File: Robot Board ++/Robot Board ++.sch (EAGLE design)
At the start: 39 parts

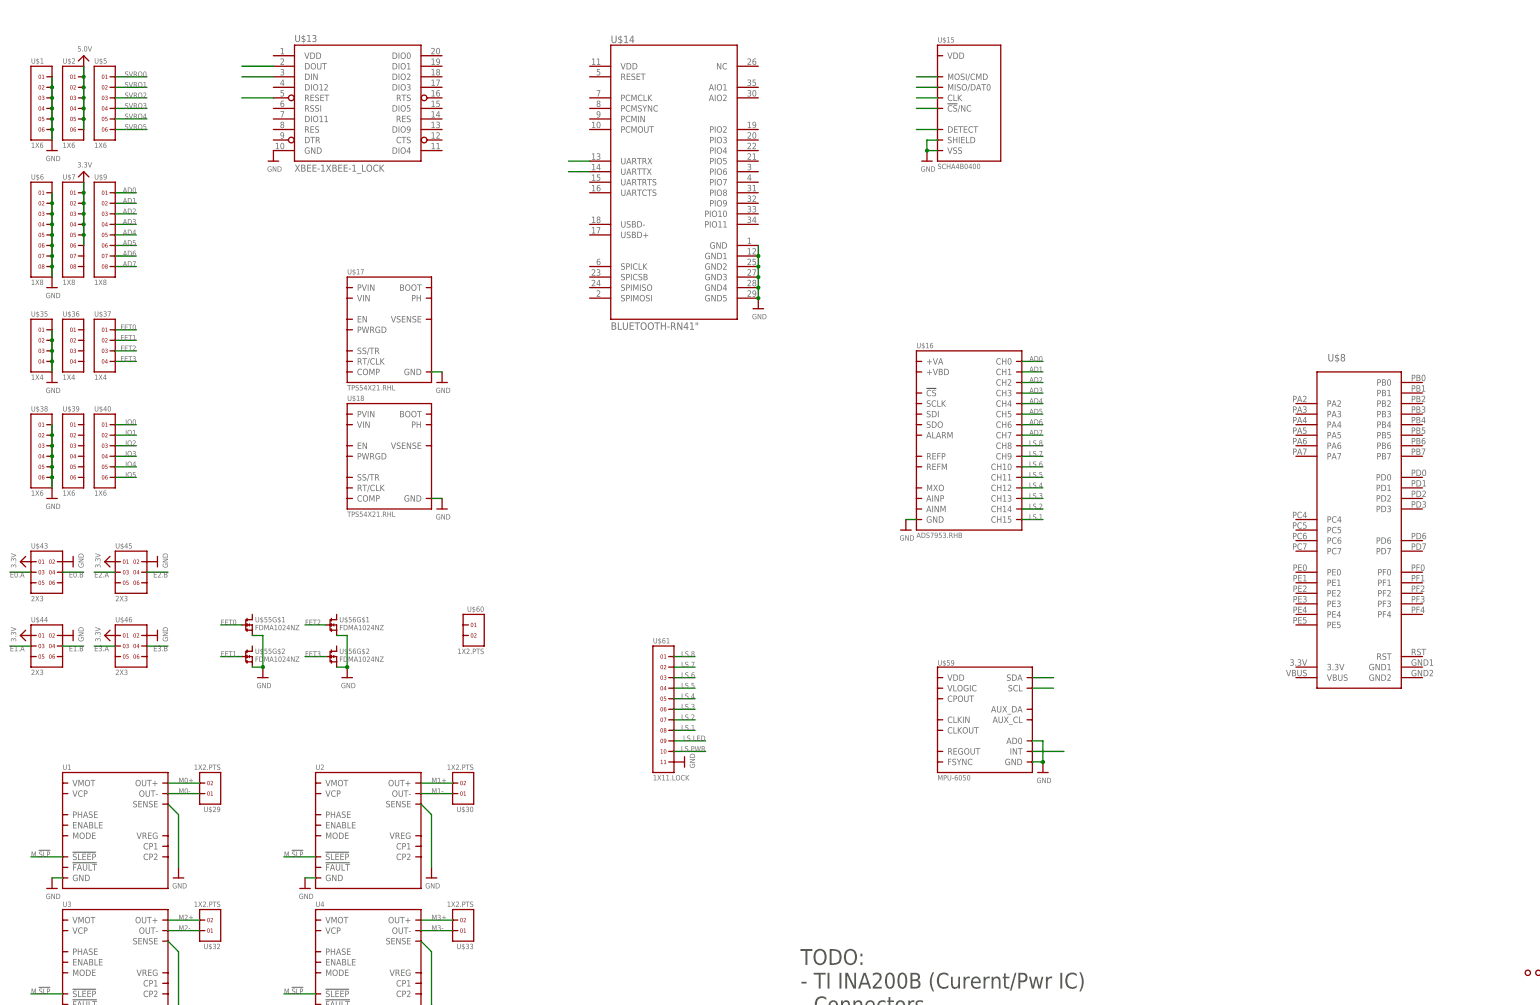
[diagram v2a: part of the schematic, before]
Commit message: Completed schematic of Vbatt -> 5v regulator Began board layout of Vbatt -> 5v regulator
Considering bringing down max current supply from 8A to 6A (footprint for XAL1010 is large)

Switched to 11-pin header for Line Sensor
Created power select jumpters
Named serial signals
Added power supply signals
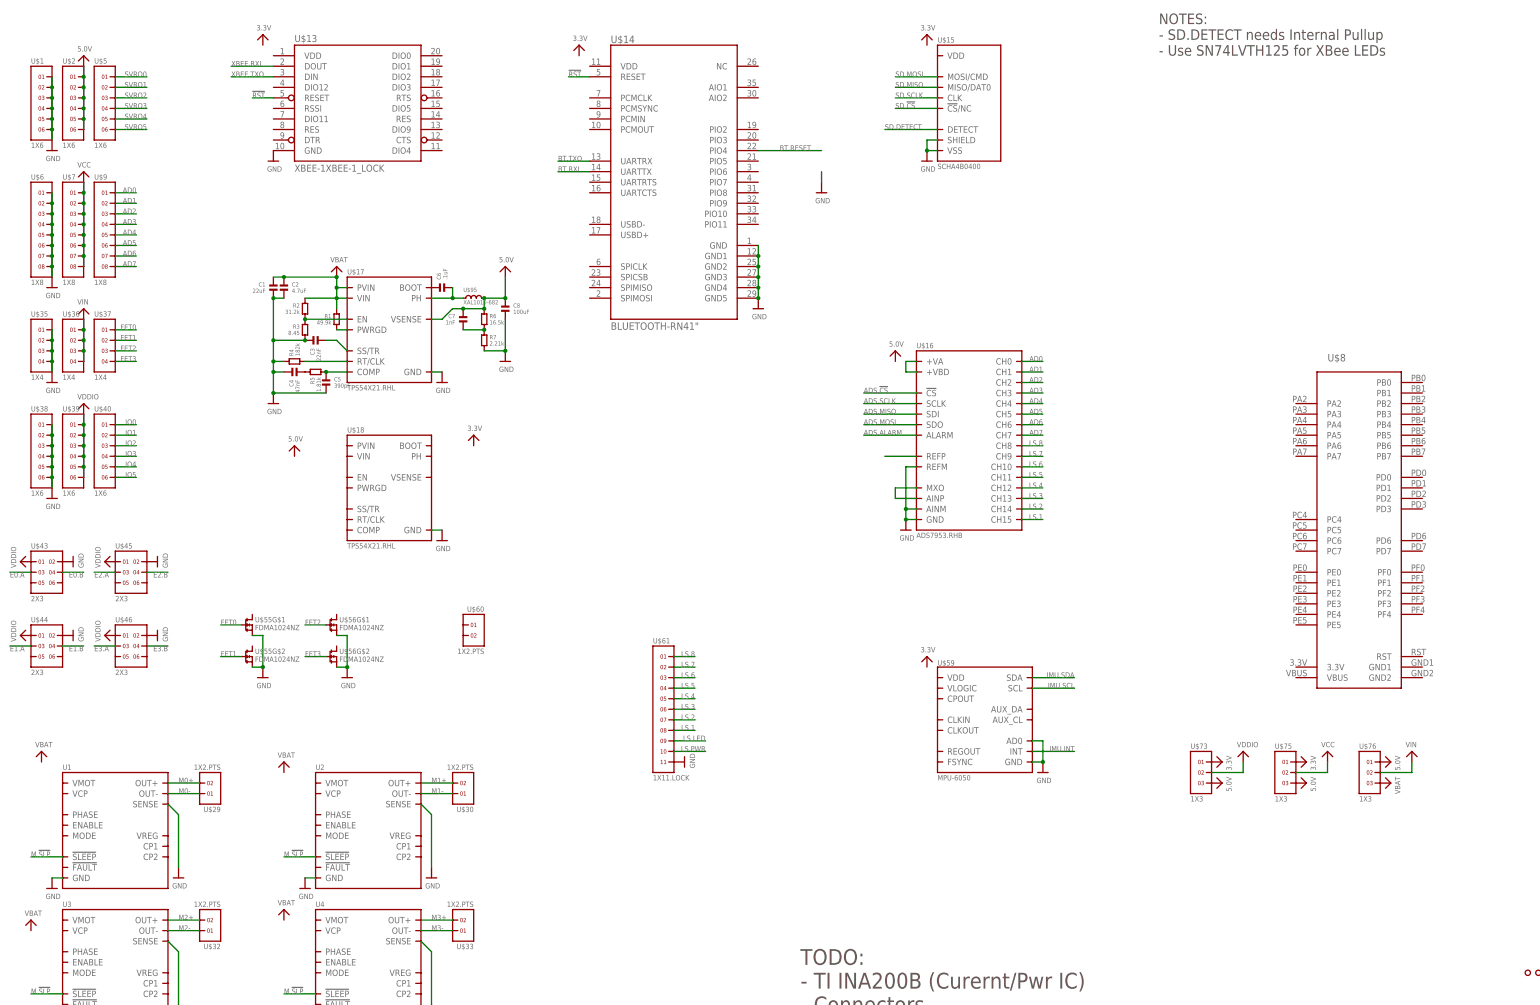
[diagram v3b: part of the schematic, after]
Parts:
- added C1: 22uF, standardparts:CAPACITOR.1206
- added C2: 4.7uF, standardparts:CAPACITOR.0805
- added C3: 22nF, standardparts:CAPACITOR.0603
- added C4: 47nF, standardparts:CAPACITOR.0603
- added C5: 390pF, standardparts:CAPACITOR.0603
- added C6: .1uF, standardparts:CAPACITOR.0603
- added C7: 1nF, standardparts:CAPACITOR.0603
- added C8: 100uF, standardparts:CAPACITOR.1210
- added R1: 49.9k, standardparts:RESISTOR.0603
- added R2: 31.2k, standardparts:RESISTOR.0603
- added R3: 8.45, standardparts:RESISTOR.0603
- added R4: 182k, standardparts:RESISTOR.0603
- added R5: 1.81k, standardparts:RESISTOR.0603
- added R6: 16.5k, standardparts:RESISTOR.0603
- added R7: 2.21k, standardparts:RESISTOR.0603
- added U$73, U$75, U$76: 1X3, headers(2mm):1X3
- added U$95: XAL1010-682, coilcraft:XAL1010-682
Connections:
- net N$1 renamed IMU.SDA
- net N$19 renamed BT.TXO
- net N$2 renamed IMU.SCL
- net N$20 renamed IMU.INT
- net N$21 renamed BT.RXI
- net N$22 renamed SD.DETECT
- net N$23 renamed SD.!CS
- net N$24 renamed SD.SCLK
- net N$25 renamed SD.MISO
- net N$26 renamed SD.MOSI
- net N$3 renamed XBEE.RXI
- net N$4 renamed XBEE.TXO
- new net !RST: U$13.RESET, U$14.RESET
- new net ADS.!CS: U$16.!CS
- new net ADS.ALARM: U$16.ALARM
- new net ADS.MISO: U$16.SDI
- new net ADS.MOSI: U$16.SDO
- new net ADS.SCLK: U$16.SCLK
- new net BT.RESET: U$14.PIO4
- new net N$1: R2.2, R3.1, U$17.EN
- new net N$10: C6.2, U$17.PH, U$95.1
- new net N$12: C7.2, R6.2, R7.1
- new net N$13: U$16.REFP
- new net N$2: R1.2, U$17.PWRGD
- new net N$3: C4.2, R5.1
- new net N$4: C5.1, R5.2, U$17.COMP
- new net N$6: U$16.AINP, U$16.MXO
- new net N$7: U$16.+VA, U$16.+VBD
- new net N$8: R4.2, U$17.RT/CLK
- new net N$9: C6.1, U$17.BOOT
- new net VBAT: C1.1, C2.1, R1.1, R2.1, U$17.PVIN, U$17.VIN, U$76.3
- new net VCC: U$7.1, U$7.2, U$7.3, U$7.4, U$7.5, U$7.6, U$7.7, U$7.8, U$75.2
- new net VDDIO: U$39.1, U$39.2, U$39.3, U$39.4, U$39.5, U$39.6, U$43.1, U$44.1, U$45.1, U$46.1, U$73.2
- new net VIN: U$36.1, U$36.2, U$36.3, U$36.4, U$76.2
- net 3.3V: now also U$73.1, U$75.1; no longer U$43.1, U$44.1, U$45.1, U$46.1, U$7.1, U$7.2, U$7.3, U$7.4, U$7.5, U$7.6
- net 5.0V: now also C7.1, C8.1, R6.1, U$17.VSENSE, U$73.3, U$75.3, U$76.1, U$95.2
- net GND: now also C1.2, C2.2, C3.1, C4.1, C5.2, C8.2, R3.2, R4.1, R7.2, U$16.AINM, U$16.REFM
- net N$5: now also C3.2, U$17.SS/TR; no longer U$13.RESET
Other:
- note added: "NOTES: - SD.DETECT needs Internal Pullup - Use SN74LVTH125 for XBee LEDs"
- moved on the sheet: U$18

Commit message: Nearly completed Schematic layout Components on board are being arranged Upgraded to TPS53319 (14A w/ smaller Inductor) Need to find more IO for GPIO pins (consider using PCA9534 IO Expander) Most passives added Added INA220 Power monitor Considering using a buffer for signals (Card Detect, XBee, Bluetooth, Power Good, etc...)
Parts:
- removed R4: 182k, standardparts:RESISTOR.0603
- removed R5: 1.81k, standardparts:RESISTOR.0603
- removed R6: 16.5k, standardparts:RESISTOR.0603
- removed R7: 2.21k, standardparts:RESISTOR.0603
- removed U$16: ADS7953.RHB, packages(ti):ADS7953.RHB
- removed U$17, U$18: TPS54X21.RHL, packages(ti):TPS54X21.RHL
- added C10: 4.7uF, standardparts:CAPACITOR.0805
- added C11, C15, C35, C37: 1uF, standardparts:CAPACITOR.0603
- added C12, C17, C19, C20, C21, C23, C24, C25, C26, C27, C28, C29, C30, C31, C33, C34, C36, C38, C39: .1uF, standardparts:CAPACITOR.0603
- added C13: 1nF, standardparts:CAPACITOR.0603
- added C14: 100uF, standardparts:CAPACITOR.1210
- added C16, C18: 100uF, microbuilder:CAP_ELECTROLYTICPANASONIC_C
- added C22, C32: 10nF, standardparts:CAPACITOR.0603
- added C9: 22uF, standardparts:CAPACITOR.1206
- added D1: (no value), nxp:DIODE[SCHOTKY]-SOD123W
- added J1, J2, J3, J4: (no value), solderjumper:SOLDERJUMPER.2.LRG
- added J5, J6, J7, J8: (no value), solderjumper:SOLDERJUMPER.2.MED
- added L1: 2.2uH, coilcraft:INDUCTOR.XAL6030
- added L2: 1uH, bourns:INDUCTOR-SRN3015
- added R10: 1k, standardparts:RESISTOR.0603
- added R11, R12: 100k, standardparts:RESISTOR.0603
- added R13: 191k, standardparts:RESISTOR.0603
- added R14: 2.55k, standardparts:RESISTOR.0603
- added R15: 76.8k, standardparts:RESISTOR.0603
- added R16: 10k, standardparts:RESISTOR.0603
- added R8: 200k, standardparts:RESISTOR.0603
- added R9: 86.6k, standardparts:RESISTOR.0603
- added U$107: 1X2, headers(.1in):1X2
- added U$118: INA220.DGS, packages(ti):INA220.DGS
- added U$98: ADS7959.RGE, packages(ti):ADS7959.RGE
- added U5: TPS5331[8/9].DQP, packages(ti):TPS5331[8/9].DQP
- C1: value 22uF -> .1uF; device standardparts:CAPACITOR.1206 -> standardparts:CAPACITOR.0603
- C2: value 4.7uF -> 10uF; device standardparts:CAPACITOR.0805 -> standardparts:CAPACITOR.0603
- C3: value 22nF -> 22uF
- C4: value 47nF -> .1uF
- C5: value 390pF -> 1uF
- C7: value 1nF -> 1uF
- C8: value 100uF -> .1uF; device standardparts:CAPACITOR.1210 -> standardparts:CAPACITOR.0603
- R1: value 49.9k -> 178k
- R2: value 31.2k -> 100k
- R3: value 8.45 -> 1u; device standardparts:RESISTOR.0603 -> vishay:RESISTOR.WSK
- U$1, U$2, U$5: value 1X6 -> 1X8; device headers(.1in):1X6 -> headers(.1in):1X8
- U$6, U$7, U$9: value 1X8 -> 1X6; device headers(.1in):1X8 -> headers(.1in):1X6
- U$95: value XAL1010-682 -> TPS62082.DSG; device coilcraft:XAL1010-682 -> packages(ti):TPS6208X.DSG
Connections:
- removed net AD6: U$16.CH6, U$9.7
- removed net AD7: U$16.CH7, U$9.8
- removed net LS.PWR: U$61.10
- removed net M.!SLP: U1.!SLEEP, U2.!SLEEP, U3.!SLEEP, U4.!SLEEP
- new net 3.3V.PG: R1.1, U$95.PG
- new net 5V.PG: R11.2, U$95.EN, U5.PGOOD
- new net M.EN: R2.1, U1.!SLEEP, U2.!SLEEP, U3.!SLEEP, U4.!SLEEP
- new net M.MODE: U1.MODE, U2.MODE, U3.MODE, U4.MODE
- new net M0.DIR: J6.1, U1.ENABLE
- new net M0.SPD: J5.1, U$8.PD0, U1.PHASE
- new net M1.DIR: J6.2, U2.ENABLE
- new net M1.SPD: J5.2, U$8.PD1, U2.PHASE
- new net M2.DIR: J8.1, U3.ENABLE
- new net M2.SPD: J7.1, U$8.PA6, U3.PHASE
- new net M3.DIR: J8.2, U4.ENABLE
- new net M3.SPD: J7.2, U$8.PA7, U4.PHASE
- new net N$11: R10.1, R8.2, R9.2
- new net N$14: C12.1, C13.2, R14.2
- new net N$15: C1.2, L1.1, R14.1, U5.LL
- new net N$16: U$8.PA4
- new net N$17: U$8.PA5
- new net N$18: C24.2, U1.VCP
- new net N$19: C25.2, U2.VCP
- new net N$20: C26.2, U3.VCP
- new net N$21: C27.2, U4.VCP
- new net N$22: D1.2, R3.1, U$118.VIN+, U$60.1
- new net N$24: C32.1, U$59.CPOUT
- new net N$25: C19.1, U2.CP2
- new net N$27: C21.1, U3.CP2
- new net N$29: C23.1, U4.CP2
- new net N$30: U$8.PF4
- new net N$31: U$8.PF3
- new net N$32: U$8.PF2
- new net N$33: U$8.PF1
- new net N$34: U$8.PF0
- new net N$37: C21.2, U3.CP1
- new net N$38: C17.2, U1.CP1
- new net N$39: C19.2, U2.CP1
- new net N$40: C23.2, U4.CP1
- new net N$44: U$8.PB3
- new net N$45: U$8.PB2
- new net N$46: U$8.PB0
- new net N$47: U$8.PB1
- new net SCL: U$118.SCL
- new net SDA: U$118.SDA
- new net SVRO6: U$5.7, U$8.PC4
- new net SVRO7: U$5.8, U$8.PC5
- new net XBEE.RSSI: U$13.RSSI
- net 3.3V: now also C15.1, C20.1, C22.1, C3.1, C38.1, C39.1, C4.1, C5.1, C6.1, C7.1, C8.1, L2.2, R1.2, U$118.VS, U$13.VDD, U$14.VDD, U$15.VDD, U$59.VDD, U$59.VLOGIC, U$7.1, U$7.2, U$7.3, U$7.4, U$7.5, U$7.6, U$95.VOS, U$98.+VBD
- net 5.0V: now also C12.2, C14.1, C2.1, L1.2, R15.1, U$107.1, U$2.7, U$2.8, U$95.VIN; no longer C7.1, C8.1, R6.1, U$17.VSENSE, U$95.2
- net AD0: now also U$8.PE3; no longer U$16.CH0
- net AD1: now also U$8.PE2; no longer U$16.CH1
- net AD2: now also U$8.PE1; no longer U$16.CH2
- net AD3: now also U$8.PE0; no longer U$16.CH3
- net AD4: now also U$8.PD3; no longer U$16.CH4
- net AD5: now also U$8.PD2; no longer U$16.CH5
- net ADS.!CS: now also U$98.!CS; no longer U$16.!CS
- net ADS.ALARM: now also U$98.ALARM; no longer U$16.ALARM
- net ADS.MISO: now also U$98.SDI; no longer U$16.SDI
- net ADS.MOSI: now also U$98.SDO; no longer U$16.SDO
- net ADS.SCLK: now also U$98.SCLK; no longer U$16.SCLK
- net BT.RXI: now also U$8.PD6
- net BT.TXO: now also U$8.PD7
- net GND: now also C10.2, C11.1, C14.2, C15.2, C16.-, C18.-, C20.2, C22.2, C24.1, C25.1, C26.1, C27.1, C28.2, C29.2, C3.2, C30.2, C31.2, C32.2, C33.1, C34.2, C35.2, C36.2, C37.2, C38.2, C39.2, C4.2, C6.2, C7.2, C9.2, D1.1, R12.1, R13.2, R16.2, R2.2, R9.1, U$1.7, U$1.8, U$107.2, U$118.A0, U$118.A1, U$118.GND, U$59.CLKIN, U$59.FSYNC, U$60.2, U$95.GND, U$95.MODE, U$98.AINM, U$98.GND, U$98.REFM, U5.GND; no longer C1.2, C3.1, C4.1, R3.2, R4.1, R7.2, U$16.AINM, U$16.GND, U$16.REFM, U$17.GND, U$18.GND, U$6.7, U$6.8
- net LS.1: now also U$98.CH7; no longer U$16.CH15
- net LS.2: now also U$98.CH6; no longer U$16.CH14
- net LS.3: now also U$98.CH5; no longer U$16.CH13
- net LS.4: now also U$98.CH4; no longer U$16.CH12
- net LS.5: now also U$98.CH3; no longer U$16.CH11
- net LS.6: now also U$98.CH2; no longer U$16.CH10
- net LS.7: now also U$98.CH1; no longer U$16.CH9
- net LS.8: now also U$98.CH0; no longer U$16.CH8
- net M0+: now also J1.1
- net M0-: now also J2.1
- net M1+: now also J1.2
- net M1-: now also J2.2
- net M2+: now also J3.1
- net M2-: now also J4.1
- net M3+: now also J3.2
- net M3-: now also J4.2
- net N$1: now also U$8.PA2; no longer R2.2, R3.1, U$17.EN
- net N$10: now also C13.1, R15.2, R16.1, U5.FB; no longer C6.2, U$17.PH, U$95.1
- net N$12: now also L2.1, U$95.SW; no longer C7.2, R6.2, R7.1
- net N$13: now also C17.1, U1.CP2; no longer U$16.REFP
- net N$2: now also C1.1, U5.VBST; no longer R1.2, U$17.PWRGD
- net N$3: now also R12.2, U5.MODE; no longer C4.2, R5.1
- net N$4: now also C11.2, R11.1, U5.VREG; no longer C5.1, R5.2, U$17.COMP
- net N$5: now also R13.1, U5.TRIP; no longer C3.2, U$17.SS/TR
- net N$6: now also U$98.AINP, U$98.MXO; no longer U$16.AINP, U$16.MXO
- net N$7: now also C33.2, U$59.REGOUT; no longer U$16.+VA, U$16.+VBD
- net N$8: now also R10.2, U5.EN; no longer R4.2, U$17.RT/CLK
- net N$9: now also U$8.PA3; no longer C6.1, U$17.BOOT
- net SVRO0: now also U$8.PB6
- net SVRO1: now also U$8.PB7
- net SVRO2: now also U$8.PB4
- net SVRO3: now also U$8.PB5
- net SVRO4: now also U$8.PE4
- net SVRO5: now also U$8.PE5
- net VBAT: now also C10.1, C16.+, C18.+, C28.1, C29.1, C30.1, C31.1, C9.1, R3.2, R8.1, U$118.VBUS, U$118.VIN-, U1.VMOT, U2.VMOT, U3.VMOT, U4.VMOT, U5.VDD, U5.VIN; no longer C1.1, C2.1, R1.1, R2.1, U$17.PVIN, U$17.VIN
- net VCC: now also C34.1, C35.1, C36.1, C37.1, U$61.10, U$98.+VA, U$98.REFP; no longer U$7.1, U$7.2, U$7.3, U$7.4, U$7.5, U$7.6, U$7.7, U$7.8
- net VIN: now also U$55G$1.D, U$56G$1.D
- net XBEE.RXI: now also U$8.PC6
- net XBEE.TXO: now also U$8.PC7
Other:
- note added: "NOTES: - SD.DETECT needs Internal Pullup - Use SN74LVTH125 for XBee LEDs - Remove R9 & R10 to decouple B[6/7] from D[0/1]"
- note added: "TODO: - Connectors - Reset - Look into Hex Non-Inverting Buffer for Status LEDs - Map Pins - Encoders - Motor GPIO - Find more GPIO Pins"
- note removed: "NOTES: - SD.DETECT needs Internal Pullup - Use SN74LVTH125 for XBee LEDs"
- note removed: "TODO: - TI INA200B (Curernt/Pwr IC) - Connectors - Reset"
- moved on the sheet: C1, C2, C3, C4, C5, C6, C7, C8, R1, R2, R3, U$29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

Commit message: Schematic tenatively completed. Changed Encoders to SPI (AS5050) Went down from 4 to 2 MOSFETs Went down from 16 to 6 IO Using 8 ADC to I2C converter for line sensor Pinouts finalized. Added indicator LEDs for debugging purposes.
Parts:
- removed U$56: FDMA1024NZ, freescale:FDMA1024NZ
- removed U$98: ADS7959.RGE, packages(ti):ADS7959.RGE
- added BTN2: B3U-1000P(M)-B, omron:SPST.B3U-1000P(M)-B
- added C42: .1uF, standardparts:CAPACITOR.0603
- added LED1, LED2, LED3, LED4, LED5, LED6, LED7, LED8: (no value), standardparts:LED.0603
- added R4: 1k, standardparts:RESISTOR.0603
- added RA1, RA2: 1k, resistorarray:RA-4.0603
- added U$123: PCA9557.RGV, packages(ti):PCA9557.RGV
- added U$126: ADS7830.PW, packages(ti):ADS7830.PW
- added U$131: 2X3, headers(2mm):2X3
- added U$132: 74XX125.RGY, packages(ti):74XX125.RGY
- added U$135: 1X2, headers(.1in):1X2
- U$1, U$2, U$5: value 1X8 -> 1X6; device headers(.1in):1X8 -> headers(.1in):1X6
- U$35, U$36, U$37: value 1X4 -> 1X2; device headers(.1in):1X4 -> headers(.1in):1X2
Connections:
- removed net ADS.!CS: U$98.!CS
- removed net ADS.ALARM: U$98.ALARM
- removed net ADS.MISO: U$98.SDI
- removed net ADS.MOSI: U$98.SDO
- removed net ADS.SCLK: U$98.SCLK
- removed net E0.A: U$43.3
- removed net E0.B: U$43.4
- removed net E1.A: U$44.3
- removed net E1.B: U$44.4
- removed net E2.A: U$45.3
- removed net E2.B: U$45.4
- removed net E3.A: U$46.3
- removed net E3.B: U$46.4
- removed net FET2: U$37.3, U$56G$1.G
- removed net FET3: U$37.4, U$56G$2.G
- removed net IMU.SCL: U$59.SCL
- removed net IMU.SDA: U$59.SDA
- removed net N$1: U$8.PA2
- removed net N$16: U$8.PA4
- removed net N$17: U$8.PA5
- removed net N$30: U$8.PF4
- removed net N$31: U$8.PF3
- removed net N$32: U$8.PF2
- removed net N$33: U$8.PF1
- removed net N$34: U$8.PF0
- removed net N$9: U$8.PA3
- removed net SD.!CS: U$15.!CS!/NC
- removed net SD.DETECT: U$15.DETECT
- removed net SD.MISO: U$15.MISO/DAT0
- removed net SD.MOSI: U$15.MOSI/CMD
- removed net SD.SCLK: U$15.CLK
- removed net SVRO6: U$5.7, U$8.PC4
- removed net SVRO7: U$5.8, U$8.PC5
- new net BT.CONNECT: LED8.1, U$14.PIO5
- new net BT.STATUS: LED7.1, U$14.PIO2
- new net ENC0.!CS: U$43.5, U$8.PD6
- new net ENC1.!CS: U$45.5, U$8.PD7
- new net I2C.SCL: U$123.SCL, U$59.SCL, U$8.PB2
- new net I2C.SDA: U$123.SDA, U$59.SDA, U$8.PB3
- new net N$43: LED2.1, U$132.2Y
- new net N$48: LED5.2, RA2.4.1
- new net N$49: LED4.2, RA1.1.2
- new net N$50: LED3.1, U$132.3Y
- new net N$51: LED1.2, RA1.4.2
- new net N$52: LED2.2, RA1.3.2
- new net N$53: LED3.2, RA1.2.2
- new net SPI.FSS: U$15.!CS!/NC, U$8.PA3
- new net SPI.MISO: U$15.MISO/DAT0, U$43.4, U$44.4, U$45.4, U$46.4, U$8.PA2
- new net SPI.MOSI: U$15.MOSI/CMD, U$43.6, U$44.6, U$45.6, U$46.6, U$8.PA5
- new net SPI.SCLK: U$15.CLK, U$43.3, U$44.3, U$45.3, U$46.3, U$8.PA4
- new net SVRO4/ENC2.!CS: U$44.5, U$8.PE4
- new net SVRO5/ENC3.!CS: U$46.5, U$8.PE5
- new net UART.RXI: U$131.3, U$132.2A, U$8.PB0
- new net UART.TXO: U$131.4, U$132.1A, U$8.PB1
- new net XBEE.ASSOCIATE: LED6.1, U$13.DIO5
- net !RST: now also U$123.!RST, U$135.1, U$8.RST
- net 3.3V: now also BTN2.2, C42.1, U$123.VCC, U$126.VDD, U$132.VCC; no longer U$98.+VBD
- net 3.3V.PG: now also U$132.4A
- net 5.0V: no longer U$2.7, U$2.8
- net 5V.PG: now also U$132.3A
- net BT.RESET: now also BTN2.1, R4.1
- net BT.RXI: now also U$131.5; no longer U$8.PD6
- net BT.TXO: now also U$131.6; no longer U$8.PD7
- net FET0: now also U$123.P6
- net FET1: now also U$123.P7
- net GND: now also C42.2, R4.2, RA1.1.1, RA1.2.1, RA1.3.1, RA1.4.1, RA2.1.1, RA2.2.2, RA2.3.2, RA2.4.2, U$123.A0, U$123.A1, U$123.A2, U$123.GND, U$126.A0, U$126.A1, U$126.COM, U$126.GND, U$132.1!OE, U$132.2!OE, U$132.3!OE, U$132.4!OE, U$132.GND, U$135.2, U$8.GND1, U$8.GND2; no longer U$1.7, U$1.8, U$35.3, U$35.4, U$56G$1.S, U$56G$2.S, U$98.AINM, U$98.GND, U$98.REFM
- net IO0: now also U$123.P0
- net IO1: now also U$123.P1
- net IO2: now also U$123.P2
- net IO3: now also U$123.P3
- net IO4: now also U$123.P4
- net IO5: now also U$123.P5
- net LS.1: now also U$126.CH0; no longer U$98.CH7
- net LS.2: now also U$126.CH1; no longer U$98.CH6
- net LS.3: now also U$126.CH2; no longer U$98.CH5
- net LS.4: now also U$126.CH3; no longer U$98.CH4
- net LS.5: now also U$126.CH4; no longer U$98.CH3
- net LS.6: now also U$126.CH5; no longer U$98.CH2
- net LS.7: now also U$126.CH6; no longer U$98.CH1
- net LS.8: now also U$126.CH7; no longer U$98.CH0
- net M0.DIR: now also U$8.PC4
- net M1.DIR: now also U$8.PC5
- net M2.DIR: now also U$8.PC6
- net M3.DIR: now also U$8.PC7
- net N$44: now also LED4.1, U$132.4Y; no longer U$8.PB3
- net N$45: now also LED8.2, RA2.1.2; no longer U$8.PB2
- net N$46: now also LED7.2, RA2.2.1; no longer U$8.PB0
- net N$47: now also LED6.2, RA2.3.1; no longer U$8.PB1
- net N$6: now also LED1.1, U$132.1Y; no longer U$98.AINP, U$98.MXO
- net SCL: now also U$126.SCL
- net SDA: now also U$126.SDA
- net SVRO4: no longer U$8.PE4
- net SVRO5: no longer U$8.PE5
- net VCC: now also U$126.REF; no longer U$98.+VA, U$98.REFP
- net VIN: no longer U$36.3, U$36.4, U$56G$1.D
- net XBEE.RSSI: now also LED5.1
- net XBEE.RXI: now also U$131.1; no longer U$8.PC6
- net XBEE.TXO: now also U$131.2; no longer U$8.PC7
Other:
- note added: "NOTES: - SD.DETECT needs Internal Pullup - Remove R9 & R10 to decouple B[6/7] from D[0/1]"
- note removed: "NOTES: - SD.DETECT needs Internal Pullup - Use SN74LVTH125 for XBee LEDs - Remove R9 & R10 to decouple B[6/7] from D[0/1]"
- note removed: "TODO: - Connectors - Reset - Look into Hex Non-Inverting Buffer for Status LEDs - Map Pins - Encoders - Motor GPIO - Find more GPIO Pins"
- moved on the sheet: C20, C22, C32, C33, C34, C35, C36, C37, C38, C39, C4, C5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

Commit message: Completed Schematic (tenatively...)
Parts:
- removed U$38, U$39, U$40: 1X6, headers(.1in):1X6
- added C40: .1uF, standardparts:CAPACITOR.0603
- added C41: 1uF, standardparts:CAPACITOR.0603
- added H10, H11, H12: 1X4, headers(.1in):1X4
- added R5: 100k, standardparts:RESISTOR.0603
- added R6, R7: 2.2k, standardparts:RESISTOR.0603
- J1, J2, J3, J4: device solderjumper:SOLDERJUMPER.2.LRG -> solderjumper:SOLDERJUMPER.2.XL
- renumbered U$1 to H1, U$107 to H22, U$131 to H23, U$135 to H24, U$2 to H2, U$29 to H17, U$30 to H18, U$32 to H19, U$33 to H20, U$35 to H7, U$36 to H8, U$37 to H9, U$43 to H13, U$44 to H15, U$45 to H14, U$46 to H16, U$5 to H3, U$6 to H4, U$60 to H21, U$7 to H5, U$73 to H25, U$75 to H26, U$76 to H27, U$9 to H6
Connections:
- removed net IMU.INT: U$59.INT
- removed net IO4: U$123.P4, U$40.5
- removed net IO5: U$123.P5, U$40.6
- removed net LS.LED: U$61.9
- removed net SCL: U$118.SCL, U$126.SCL
- removed net SDA: U$118.SDA, U$126.SDA
- new net I2C.SDL: U$126.SCL
- net 3.3V: now also C40.1, C41.1, R6.1, R7.1
- net 5.0V: now also U$8.VBUS
- net FET0: now also U$123.P4; no longer U$123.P6
- net FET1: now also U$123.P5; no longer U$123.P7
- net GND: now also C40.2, C41.2, H10.1, H10.2, H10.3, H10.4; no longer U$38.1, U$38.2, U$38.3, U$38.4, U$38.5, U$38.6
- net I2C.SCL: now also R6.2, U$118.SCL
- net I2C.SDA: now also R7.2, U$118.SDA, U$126.SDA
- net IO0: now also H12.1; no longer U$40.1
- net IO1: now also H12.2; no longer U$40.2
- net IO2: now also H12.3; no longer U$40.3
- net IO3: now also H12.4; no longer U$40.4
- net M.EN: now also U$123.P7
- net M.MODE: now also R5.2, U$123.P6
- net VCC: now also U$61.9
- net VDDIO: now also H11.1, H11.2, H11.3, H11.4, R5.1; no longer U$39.1, U$39.2, U$39.3, U$39.4, U$39.5, U$39.6
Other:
- note added: "NOTES: - Remove R9 & R10 to decouple B[6/7] from D[0/1] - Externals to create - SPI Encoder - Line Sensor Adapter - Adapter for Parallel Motors - Schottky Diodes"
- note removed: "NOTES: - SD.DETECT needs Internal Pullup - Remove R9 & R10 to decouple B[6/7] from D[0/1]"
- moved on the sheet: LED1, LED2, LED3, LED4, LED5, LED6, LED7, LED8, RA1.1, RA1.2, RA1.3, RA1.4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
